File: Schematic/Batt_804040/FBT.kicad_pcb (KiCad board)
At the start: 2 copper layers, 83.3 x 52 mm, 19 parts, among them J1 TRRS Connector 3.5, J2 TRRS Connector 3.5, SW1 SW_SPDT

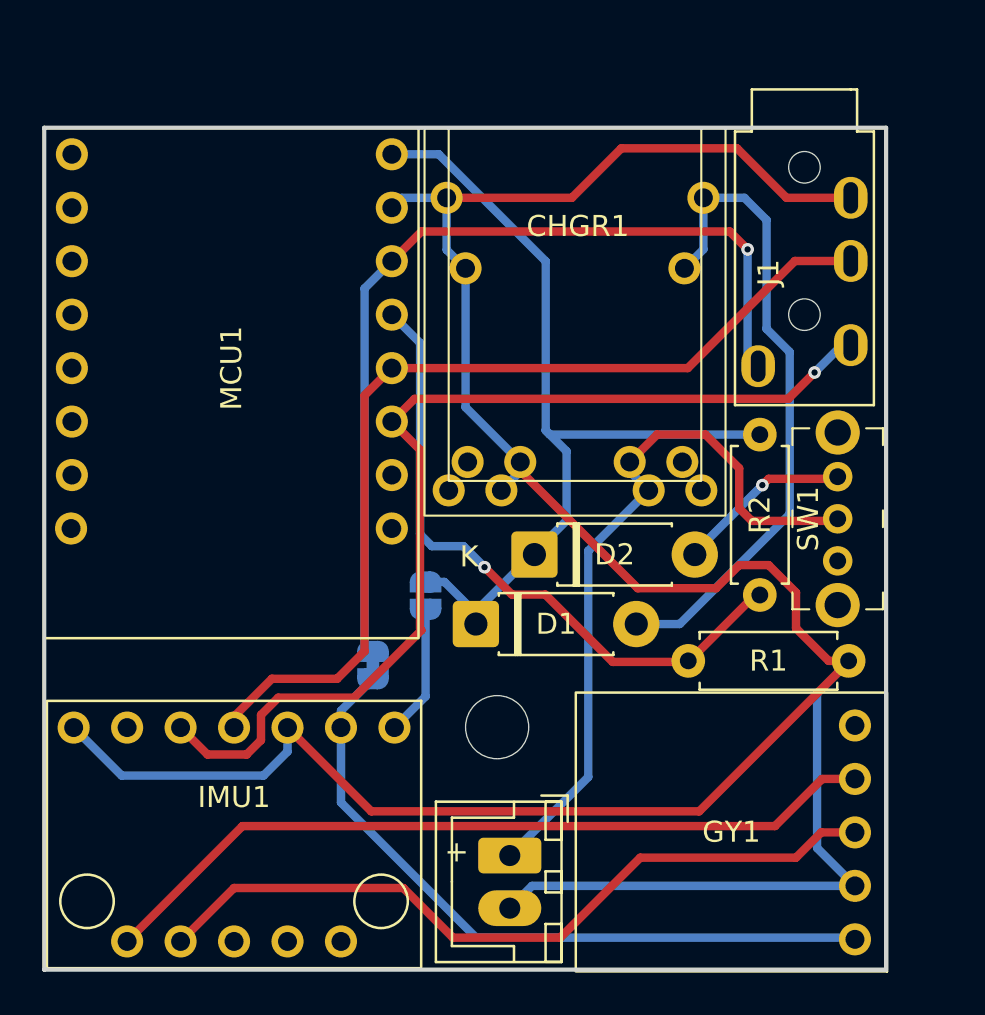
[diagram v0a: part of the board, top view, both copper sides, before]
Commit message: Update schematic to v3
Added support for a discrete LDO (HT7333) so we can correct the bodge we did with the original design.
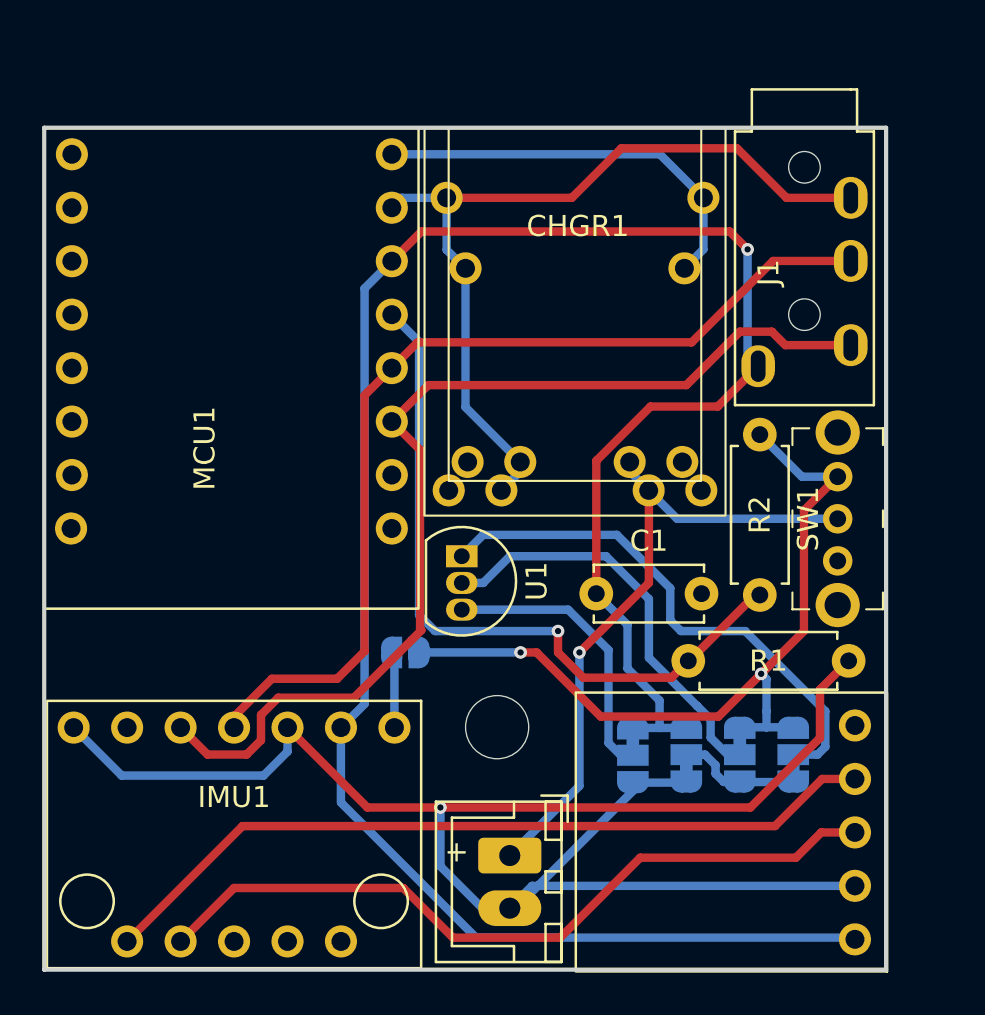
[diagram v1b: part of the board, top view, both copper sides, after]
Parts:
- removed D1: D_1N5817 / 4.8v Zener?, Diode_THT:D_DO-41_SOD81_P7.62mm_Horizontal
- removed D2: D_1N5817, Diode_THT:D_DO-41_SOD81_P7.62mm_Horizontal
- removed JP2: 3v3 in, Jumper:SolderJumper-2_P1.3mm_Bridged_RoundedPad1.0x1.5mm
- added C1: 10 uF, Capacitor_THT:C_Disc_D5.0mm_W2.5mm_P5.00mm, F.Cu at (123.2, 117.9)
- added JP3: A, Jumper:SolderJumper-3_P1.3mm_Bridged12_RoundedPad1.0x1.5mm_NumberLabels, B.Cu at (132.6, 125.5)
- added JP4: D, Jumper:SolderJumper-3_P1.3mm_Bridged12_RoundedPad1.0x1.5mm_NumberLabels, B.Cu at (125.0, 125.5)
- added JP5: B, Jumper:SolderJumper-3_P1.3mm_Bridged12_RoundedPad1.0x1.5mm_NumberLabels, B.Cu at (130.0, 125.5)
- added JP6: C, Jumper:SolderJumper-3_P1.3mm_Bridged12_RoundedPad1.0x1.5mm_NumberLabels, B.Cu at (127.5, 125.5)
- added U1: HT7333-1-TO92, Package_TO_SOT_THT:TO-92L_Inline, F.Cu at (116.8, 116.1)
- JP1: value 5v in -> E
- MCU1: footprint Espressif:ESP32-C3-Mini-V1 -> Espressif:ESP32-C3-SuperMini_PLUS
- moved JP1 2.87 mm to (114.2, 120.7), turned to 0 degrees
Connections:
- CHGR1 pad 1: /5_VIN_LX -> ESP32_5V5
- CHGR2 pad 1: /5_VIN_LX -> ESP32_5V5
- GY1 pad 1: Net-(GY1-VIN) -> ESP32_3V3
- IMU1 pad 2: Net-(GY1-VIN) -> ESP32_3V3
- JP1 pad 2: ESP32_5V5 -> BATT_SWITCHED
- R2 pad 2: ESP32_5V5 -> BATT_SWITCHED
- SW1 pad 3: Net-(D2-A) -> BATT_SWITCHED
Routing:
- net ESP32_3V3: track 62.0 -> 122.6 mm
- net BATT_SWITCHED: track 0.00 -> 38.9 mm, vias 0 -> 2
- net Net-(GY1-VIN): track 33.6 -> 0.00 mm
- net /5_VIN_LX: track 30.5 -> 0.00 mm
- net /ldo_gnd: track 0.00 -> 25.4 mm
- net ESP32_5V5: track 42.5 -> 19.4 mm
- net /vin: track 0.00 -> 19.8 mm
- net GND: track 146.7 -> 132.7 mm, vias 0 -> 1
- net /vout: track 0.00 -> 13.6 mm
- net Net-(D2-A): track 8.15 -> 0.00 mm, vias 1 -> 0
- net /gnd_mid: track 0.00 -> 5.86 mm
- net +BATT: track 35.4 -> 31.8 mm, vias 0 -> 1
- net BATTERY_READER: track 30.9 -> 34.4 mm
- net Net-(IMU1-VIN): track 6.23 -> 3.37 mm
- net SDA_1: track 63.1 -> 64.0 mm, vias 1 -> 0
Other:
- board text added: "Type A Rev. 3.0"
- board text removed: "Type A Rev. 2.0"

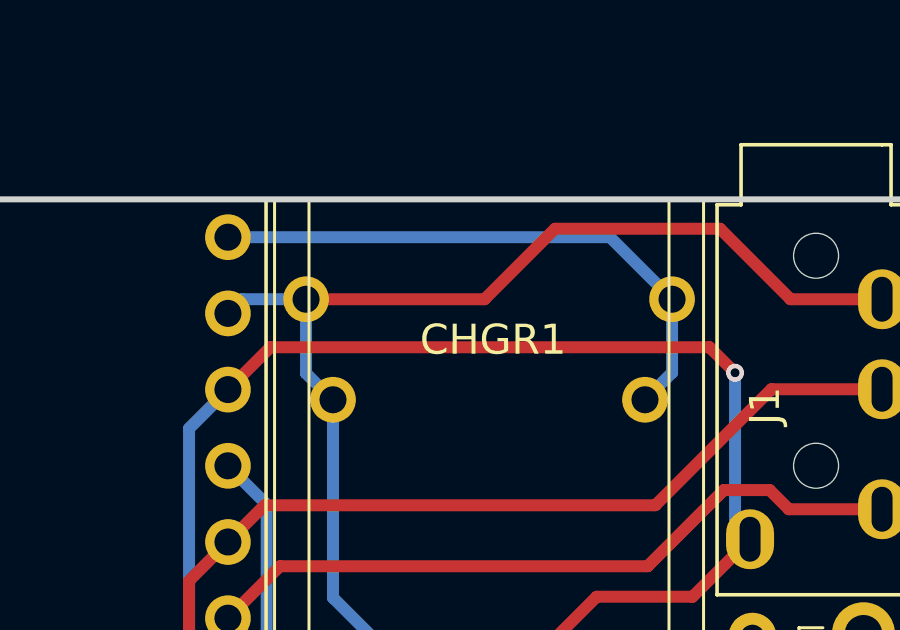
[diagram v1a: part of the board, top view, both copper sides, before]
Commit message: Slight PCB tweaking
Double-checking that everything is correct before I ship off the next batch for fabbing.
Added a jumper pad between usb-c 5v inputs.
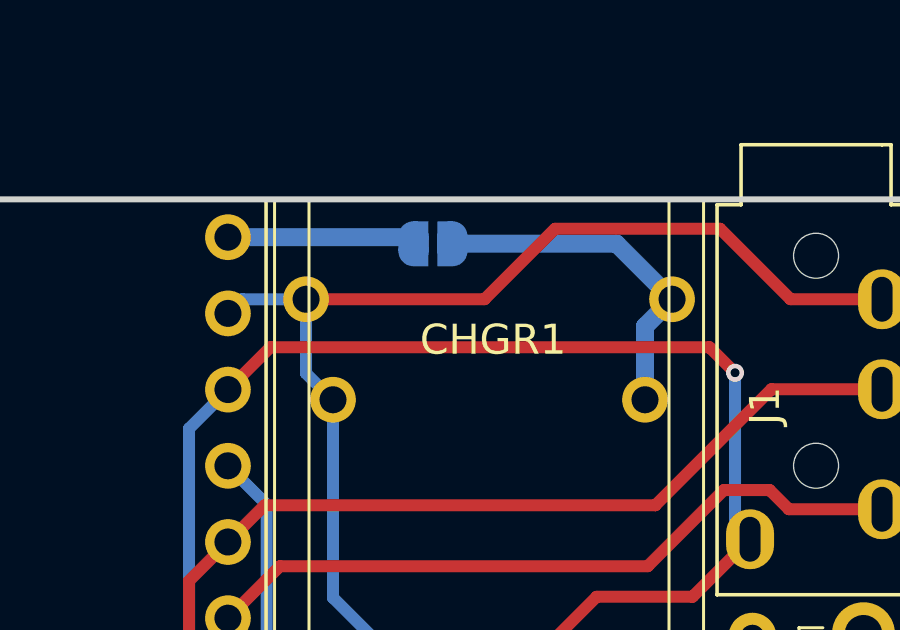
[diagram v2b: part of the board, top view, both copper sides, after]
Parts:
- added JP2: F, Jumper:SolderJumper-2_P1.3mm_Open_RoundedPad1.0x1.5mm, B.Cu at (120.3, 97.2)
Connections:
- CHGR1 pad 1: ESP32_5V5 -> Net-(CHGR1-5_VIN)
- CHGR2 pad 1: ESP32_5V5 -> Net-(CHGR1-5_VIN)
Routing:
- net ESP32_5V5: track 19.4 -> 6.27 mm
- net Net-(CHGR1-5_VIN): track 0.00 -> 11.8 mm
